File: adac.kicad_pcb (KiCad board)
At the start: 2 copper layers, 26 parts, among them J1 Conn_Coaxial, J2 Conn_Coaxial, J3 Conn_Coaxial, SW1 SW_SPST, U1 LTC1740, U2 TXS0108EPW, U3 TXS0108EPW, U4 AD7840

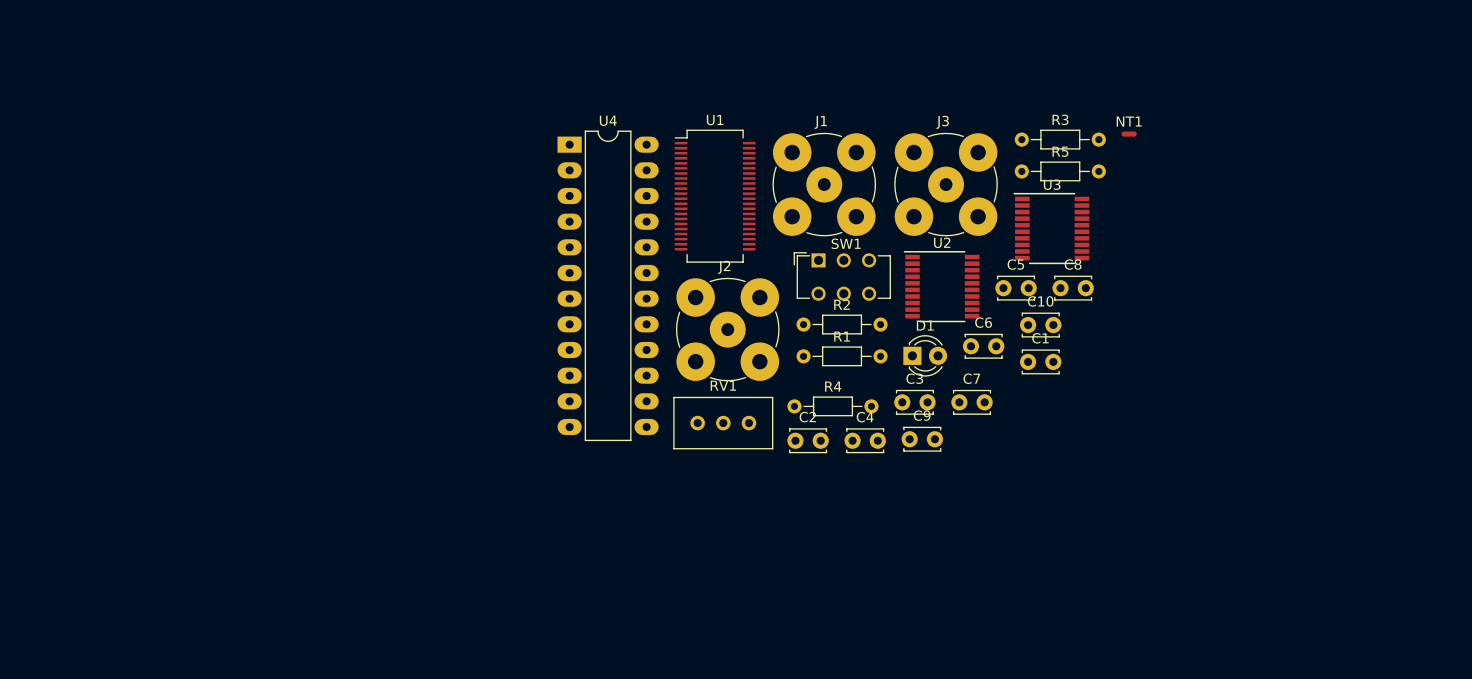
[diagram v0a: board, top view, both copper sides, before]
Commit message: Spread out components
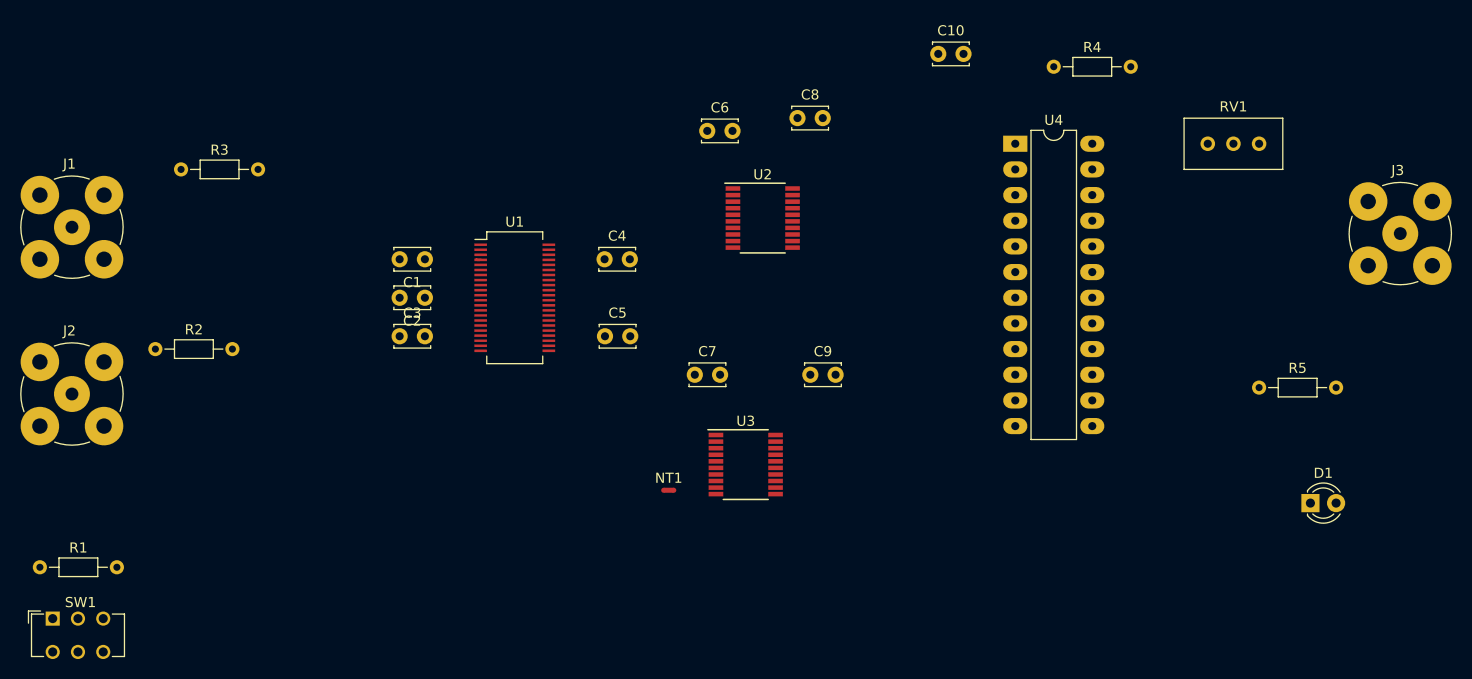
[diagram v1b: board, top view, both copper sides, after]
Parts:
- moved SW1 83.7 mm to (62.2, 128.3)
- moved R3 83.3 mm to (74.9, 83.8)
- moved R1 78.4 mm to (61.0, 123.2)
- moved J1 74.6 mm to (64.1, 89.5)
- moved J2 65.2 mm to (64.1, 106.0)
- moved R2 64.2 mm to (72.4, 101.6)
- moved C1 60.5 mm to (99.1, 92.7), turned to 180 degrees
- moved NT1 57.6 mm to (123.2, 115.6)
- moved RV1 57.6 mm to (181.6, 81.3)
- moved C3 50.2 mm to (96.6, 100.3)
- moved J3 45.2 mm to (195.6, 90.2)
- moved U4 44.1 mm to (157.5, 81.3)
- moved R4 42.3 mm to (161.3, 73.7)
- moved D1 42.0 mm to (186.7, 116.8)
- moved C5 39.7 mm to (116.9, 100.3)
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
